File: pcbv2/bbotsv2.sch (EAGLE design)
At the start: 14 parts

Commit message: connected everything to amica, not tested
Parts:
- removed LED2: WS2812B, LEDWS2812:WS2812B
- added RES1, RES2: (no value), my-library:BB-RESM0805
- added U$5: BB-USBTTL, my-library:BB-USBTTL
- LED1: value WS2812B -> (none); device LEDWS2812:WS2812B -> my-library:BB-RESM0805
- U$3: value ESP8266 -> ESP07-16PIN; device esp8266modules:ESP8266 -> esp8266modules:ESP07-16PIN
- renumbered BAT to ALIMENTACION_11.1V
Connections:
- net N$3 renamed 12V
- new net 5V: A0.5V, D1-GPIO5.5V, D2-GPIO4.5V, LED1.1, NODE1.VIN, U$4.OUT+
- new net N$17: NODE1.3V3@1, U$2.STBY, U$2.VCC
- new net N$18: D1-GPIO5.S, NODE1.D3
- new net N$3: LED1.2, RES1.2
- net N$10: now also NODE1.D1; no longer NODE1.D4
- net N$12: now also D2-GPIO4.S, NODE1.D4; no longer NODE1.D3, U$2.PWMB
- net N$19: now also U$3.TX, U$5.RX; no longer D2-GPIO4.S, NODE1.D2
- net N$20: now also U$3.RX, U$5.TX; no longer D1-GPIO5.S, NODE1.D1
- net N$4: now also NODE1.D8; no longer NODE1.D7
- net N$5: now also NODE1.D7, U$2.PWMB; no longer A0.5V, D1-GPIO5.5V, D2-GPIO4.5V, NODE1.VIN, U$2.STBY, U$2.VCC, U$4.OUT+
- net N$6: now also RES1.1, U$3.GND, U$5.GND
- net N$9: now also NODE1.D2; no longer NODE1.3V3@2

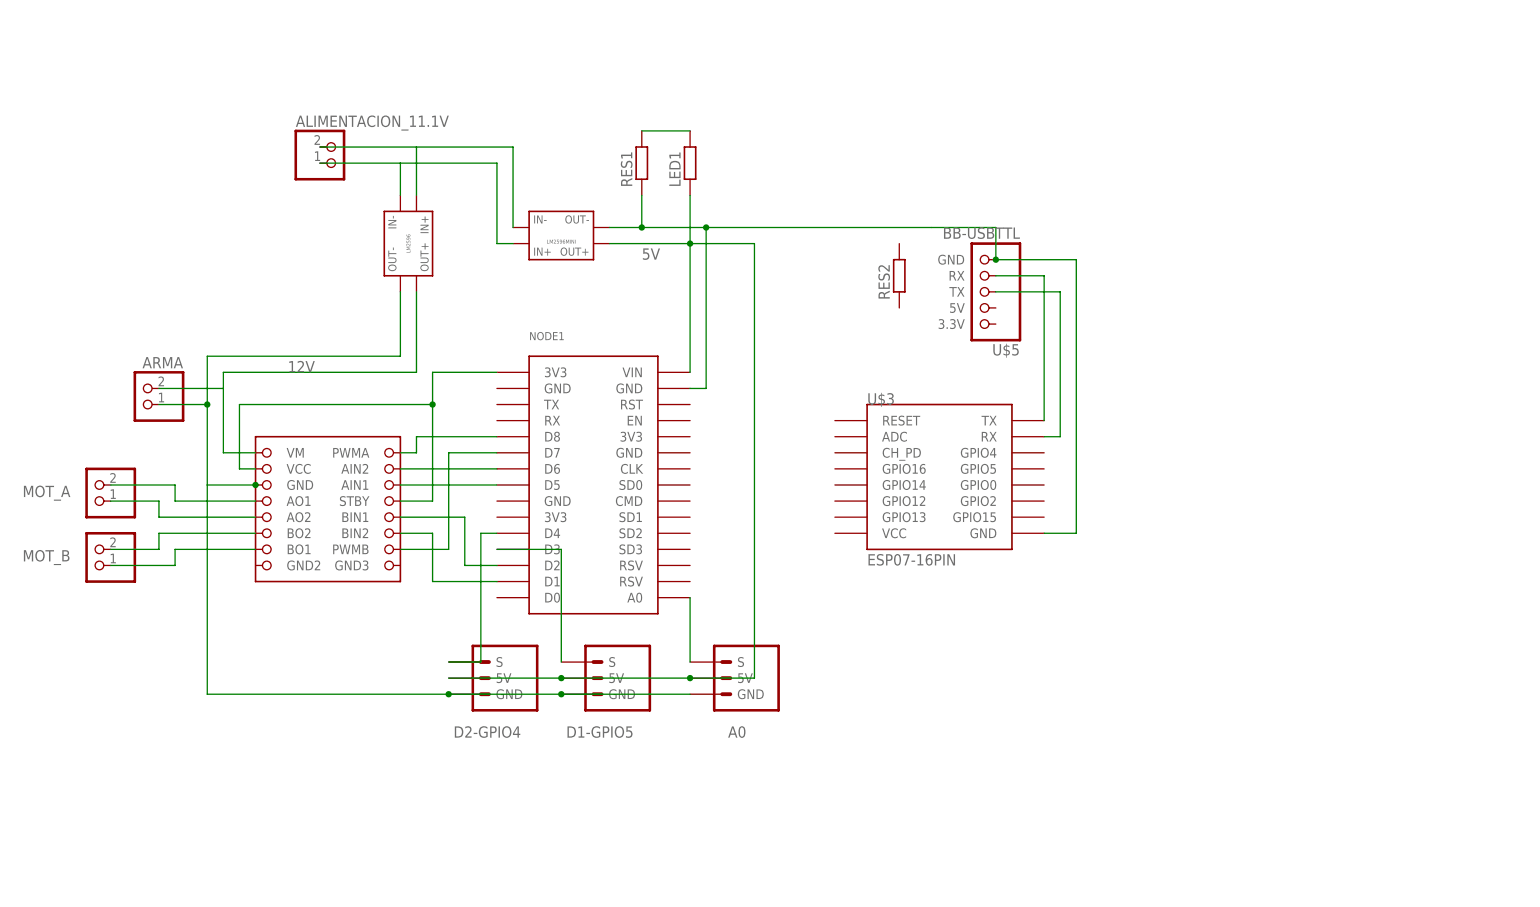
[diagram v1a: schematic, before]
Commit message: connected esp07 on schematic and ruted all components
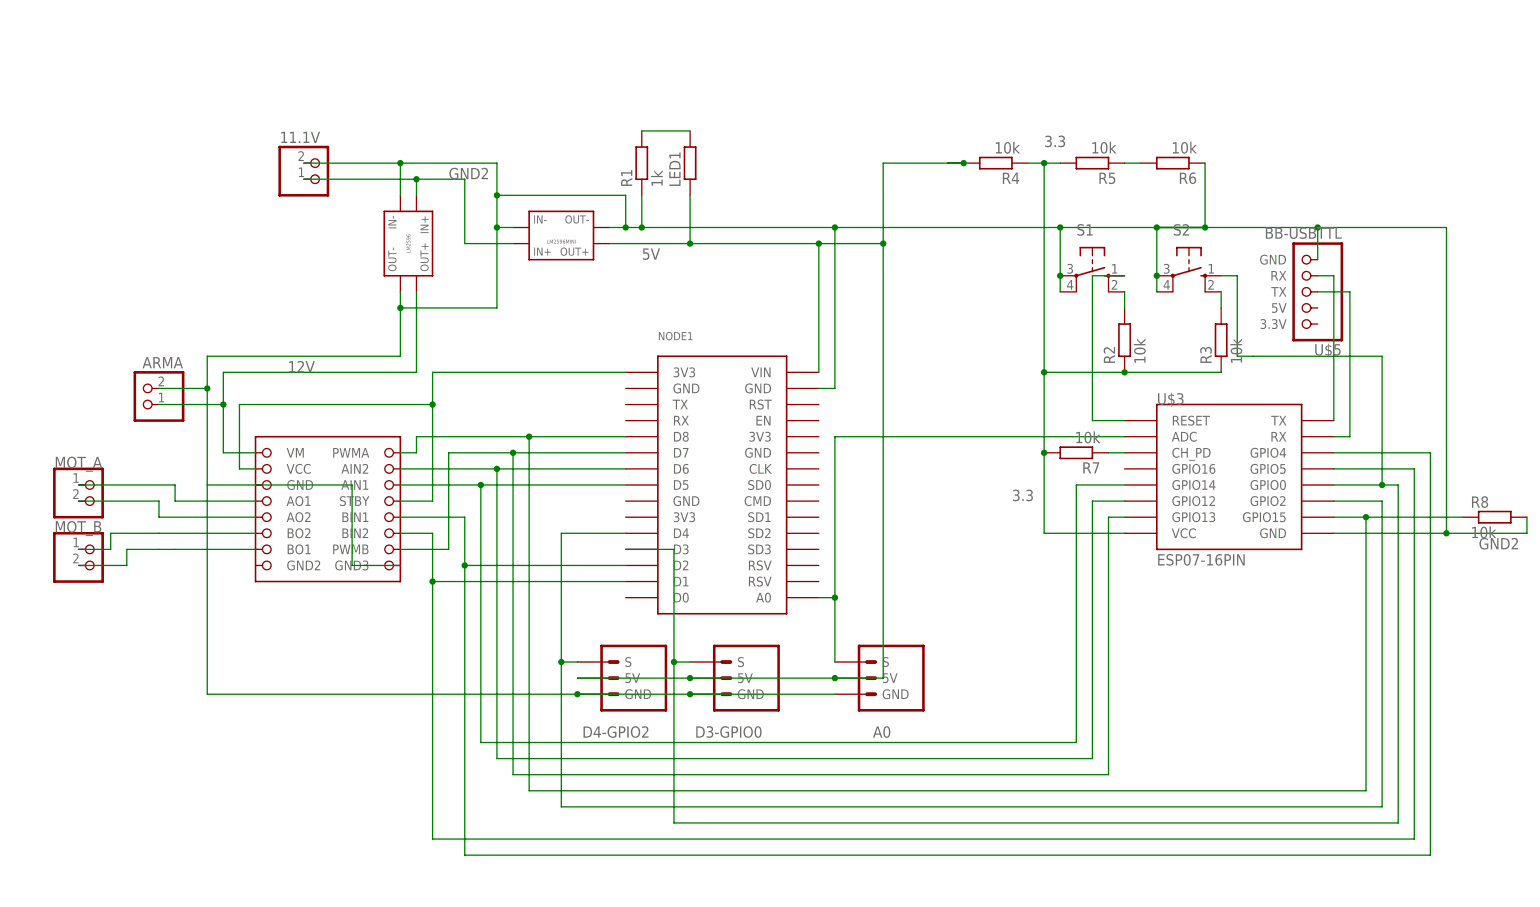
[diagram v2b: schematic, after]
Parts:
- removed ALIMENTACION_11.1V: (no value), adafruit:JST_2PIN-THM
- removed D1-GPIO5, D2-GPIO4: BB-PIN3, my-library:BB-PIN3
- removed RES2: (no value), my-library:BB-RESM0805
- added 11.1V: (no value), adafruit:JST_2PIN-THM
- added D3-GPIO0, D4-GPIO2: BB-PIN3, my-library:BB-PIN3
- added R2, R3, R4, R5, R6, R7, R8: 10k, my-library:BB-RESM0805
- added S1, S2: (no value), switch-omron:10-XX
- R1: value (none) -> 1k
- renumbered RES1 to R1
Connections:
- removed net N$11: A0.GND, ARMA.2, D1-GPIO5.GND, D2-GPIO4.GND, U$1.OUT-, U$2.GND
- removed net N$2: ALIMENTACION_11.1V.2, U$1.IN-, U$4.IN+
- removed net N$6: NODE1.GND@4, R1.1, U$3.GND, U$4.OUT-, U$5.GND
- new net 3.3: R2.1, R3.1, R4.1, R5.2, R7.2, U$3.VCC
- new net GND2: 11.1V.1, A0.GND, ARMA.1, D3-GPIO0.GND, D4-GPIO2.GND, NODE1.GND@4, R1.1, R6.1, R8.2, S1.P, S1.P1, S2.P, S2.P1, U$1.IN-, U$1.OUT-, U$2.GND, U$2.GND3, U$3.GND, U$4.IN-, U$4.OUT-, U$5.GND
- new net N$22: R2.2, S1.S1
- new net N$23: R3.2, S2.S1
- new net N$25: R5.1, R6.2
- new net N$27: S1.S, U$3.RESET
- new net N$28: R7.1, U$3.CH_PD
- net 12V: now also ARMA.2; no longer ARMA.1
- net 5V: now also D3-GPIO0.5V, D4-GPIO2.5V, R4.2; no longer D1-GPIO5.5V, D2-GPIO4.5V
- net N$1: now also 11.1V.2, U$4.IN+; no longer ALIMENTACION_11.1V.1, U$4.IN-
- net N$10: now also U$3.GPIO5
- net N$12: now also D4-GPIO2.S, U$3.GPIO2; no longer D2-GPIO4.S
- net N$13: now also MOT_A.1; no longer MOT_A.2
- net N$14: now also MOT_A.2; no longer MOT_A.1
- net N$15: now also MOT_B.2; no longer MOT_B.1
- net N$16: now also MOT_B.1; no longer MOT_B.2
- net N$18: now also D3-GPIO0.S, S2.S, U$3.GPIO0; no longer D1-GPIO5.S
- net N$21: now also U$3.ADC
- net N$4: now also R8.1, U$3.GPIO15
- net N$5: now also U$3.GPIO13
- net N$7: now also U$3.GPIO12
- net N$8: now also U$3.GPIO14
- net N$9: now also U$3.GPIO4
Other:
- moved on the sheet: A0, MOT_A, MOT_B, NODE1, U$3, U$5
